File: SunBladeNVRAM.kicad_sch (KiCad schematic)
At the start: 15 parts, among them J1 Conn_01x14_Pin, J105 Conn_01x01_Pin, J106 Conn_01x01_Pin, J107 Conn_01x01_Pin, J108 Conn_01x01_Pin, J2 Conn_01x14_Pin, J3 Conn_01x02_Pin, J4 Conn_01x02_Pin, J5 Conn_01x01_Pin, J6 Conn_01x01_Pin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

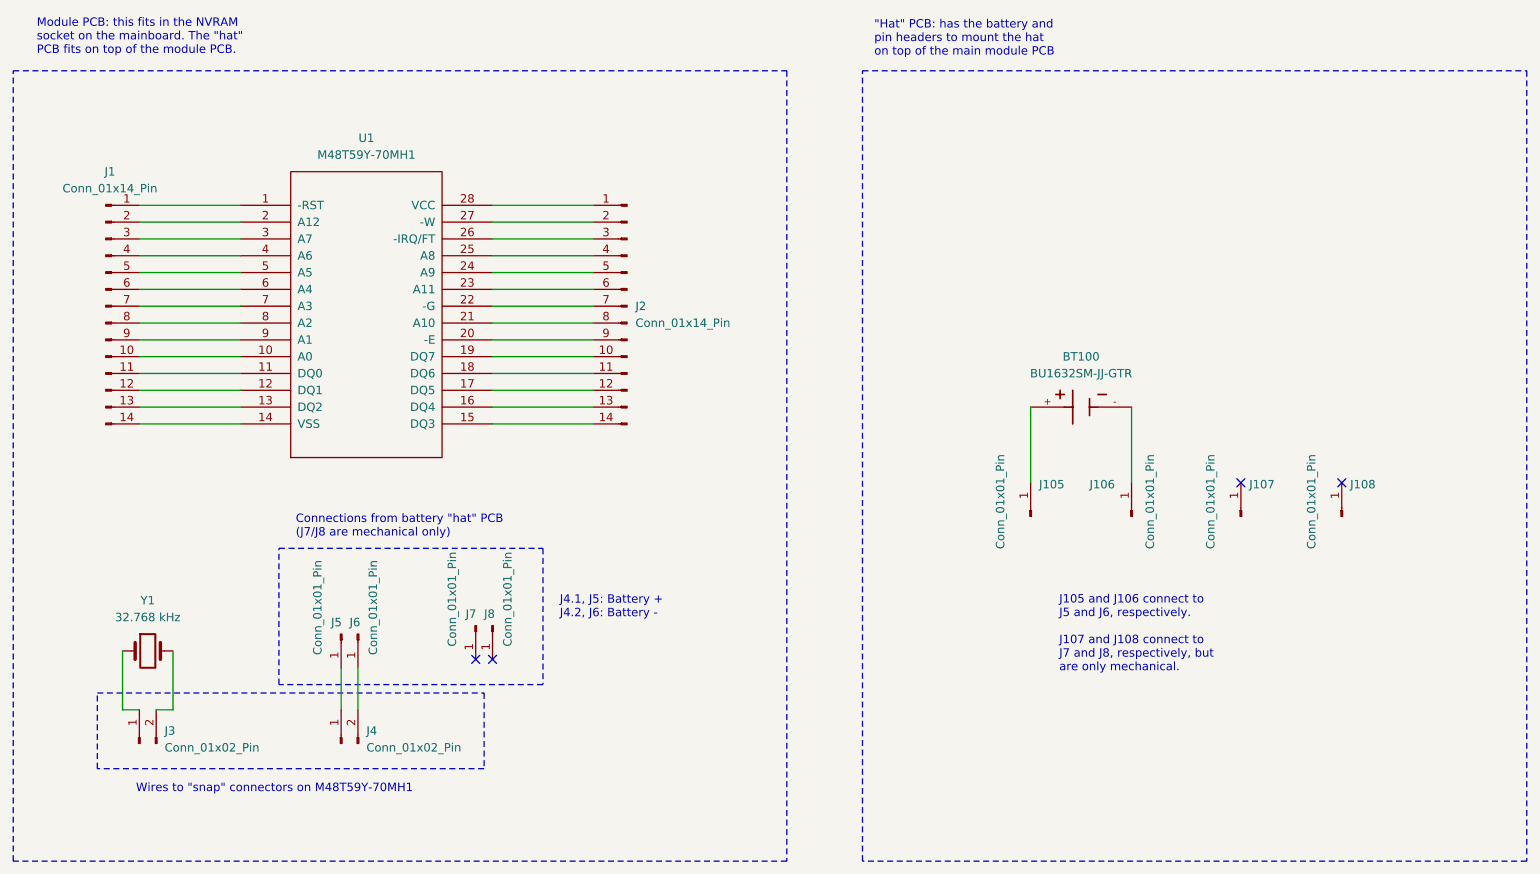
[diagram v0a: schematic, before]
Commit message: use correct M48T59Y-MH footprint
Changed pin headers to be surface mount, meaning the
pads can be on the bottom and so not interfere with the
M49T59Y.

Bottom PCB needs to be a bit larger, and the top
(battery hat) PCB also needed a minor redesign.

Still need to route the connections.
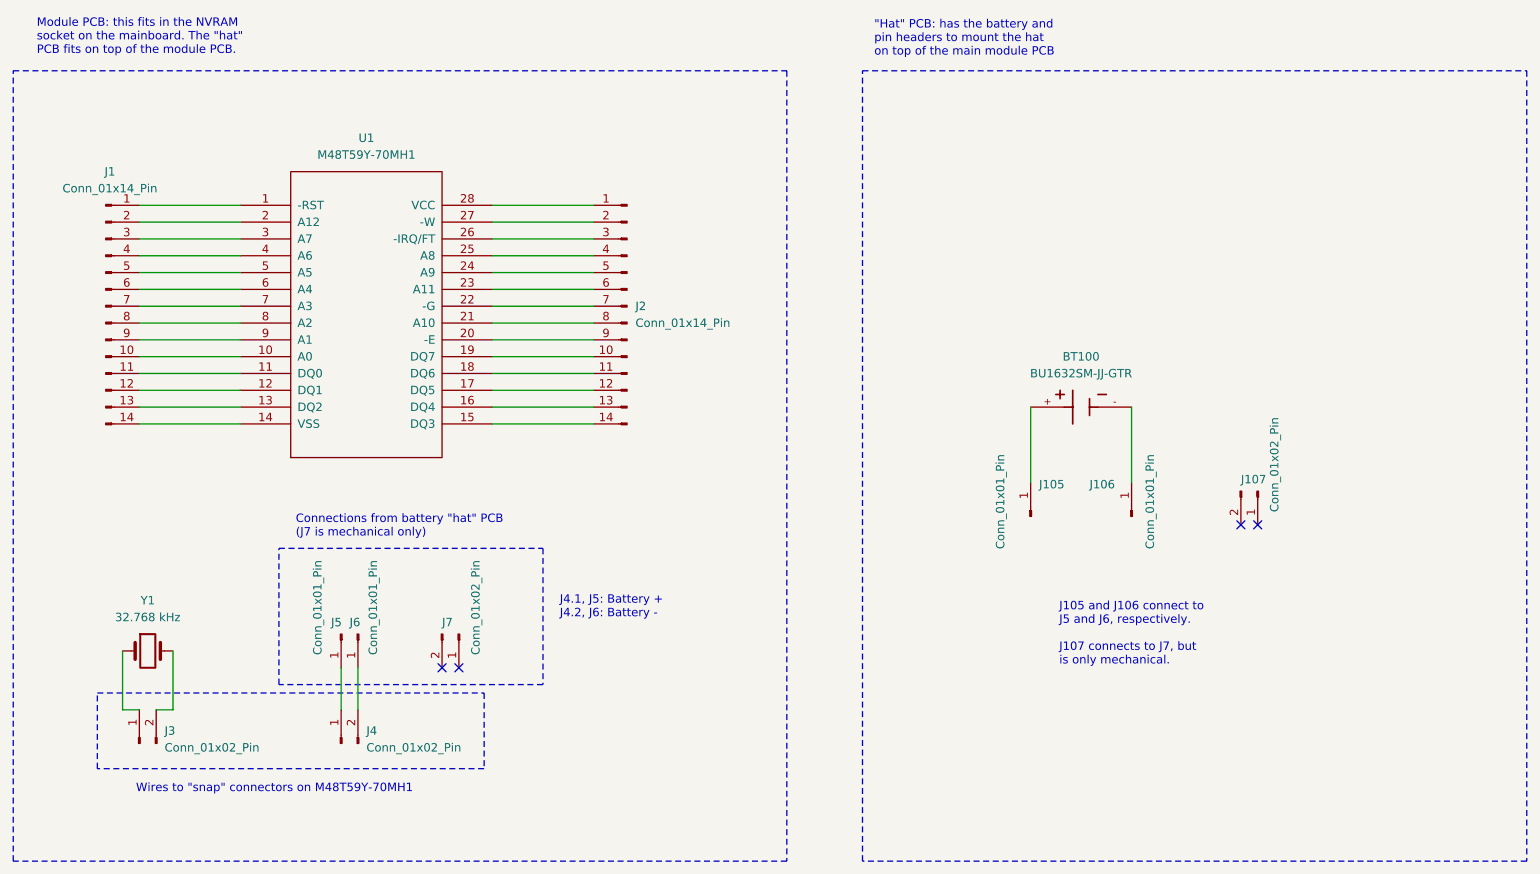
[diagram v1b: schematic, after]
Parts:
- removed J107, J108, J7, J8: Conn_01x01_Pin, Connector_PinHeader_2.54mm:PinHeader_1x01_P2.54mm_Vertical, symbol Connector:Conn_01x01_Pin
- added J107, J7: Conn_01x02_Pin, Connector_PinHeader_2.54mm:PinHeader_1x02_P2.54mm_Vertical, symbol Connector:Conn_01x02_Pin
- J1: footprint Connector_PinHeader_2.54mm:PinHeader_1x14_P2.54mm_Vertical -> Connector_PinHeader_2.54mm:PinHeader_1x14_P2.54mm_Vertical_SMD_Pin1Left
- J2: footprint Connector_PinHeader_2.54mm:PinHeader_1x14_P2.54mm_Vertical -> Connector_PinHeader_2.54mm:PinHeader_1x14_P2.54mm_Vertical_SMD_Pin1Right
- U1: footprint Package_SO:SOIC-28W_7.5x17.9mm_P1.27mm -> SunBladeNVRAM:M48T59Y-MH
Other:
- note added: "Connections from battery "hat" PCB (J7 is mechanical only)"
- note added: "J105 and J106 connect to J5 and J6, respectively. J107 connects to J7, but is only mechanical."
- note removed: "Connections from battery "hat" PCB (J7/J8 are mechanical only)"
- note removed: "J105 and J106 connect to J5 and J6, respectively. J107 and J108 connect to J7 and J8, respectively, but are only mechanical."
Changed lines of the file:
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@@
 	)
 	(no_connect
-		(at 102.87 132.08)
+		(at 215.9 111.76)
 	)
 	(no_connect
-		(at 215.9 105.41)
+		(at 218.44 111.76)
 	)
 	(no_connect
-		(at 231.14 105.41)
+		(at 95.25 133.35)
 	)
 	(no_connect
-		(at 100.33 132.08)
+		(at 97.79 133.35)
 	)
 	(wire
@@
 		)
 	)
-	(text "Connections from battery \"hat\" PCB\n(J7/J8 are mechanical only)"
+	(text "Connections from battery \"hat\" PCB\n(J7 is mechanical only)"
 		(exclude_from_sim no)
 		(at 73.152 112.014 0)
@@
 		)
 	)
-	(text "J105 and J106 connect to\nJ5 and J6, respectively.\n\nJ107 and J108 connect to\nJ7 and J8, respectively, but\nare only mechanical."
+	(text "J105 and J106 connect to\nJ5 and J6, respectively.\n\nJ107 connects to J7, but\nis only mechanical."
 		(exclude_from_sim no)
 		(at 188.468 128.27 0)
@@
 			)
 		)
-		(property "Footprint" "Connector_PinHeader_2.54mm:PinHeader_1x14_P2.54mm_Vertical"
+		(property "Footprint" "Connector_PinHeader_2.54mm:PinHeader_1x14_P2.54mm_Vertical_SMD_Pin1Left"
 			(at 44.45 78.74 0)
 			(effects
@@
 	)
 	(symbol
-		(lib_id "Connector:Conn_01x01_Pin")
-		(at 215.9 110.49 90)
+		(lib_id "Connector:Conn_01x02_Pin")
+		(at 218.44 106.68 270)
 		(unit 1)
 		(exclude_from_sim no)
@@
 		(dnp no)
 		(property "Reference" "J107"
-			(at 217.17 105.664 90)
-			(effects
-				(font
-					(size 1.27 1.27)
-				)
-				(justify right)
-			)
-		)
-		(property "Value" "Conn_01x01_Pin"
-			(at 211.328 101.092 0)
-			(effects
-				(font
-					(size 1.27 1.27)
-				)
-				(justify right)
-			)
-		)
-		(property "Footprint" "Connector_PinHeader_2.54mm:PinHeader_1x01_P2.54mm_Vertical"
-			(at 215.9 110.49 0)
+			(at 215.9 104.902 90)
+			(effects
+				(font
+					(size 1.27 1.27)
+				)
+				(justify left)
+			)
+		)
+		(property "Value" "Conn_01x02_Pin"
+			(at 220.98 95.504 0)
+			(effects
+				(font
+					(size 1.27 1.27)
+				)
+				(justify left)
+			)
+		)
+		(property "Footprint" "Connector_PinHeader_2.54mm:PinHeader_1x02_P2.54mm_Vertical"
+			(at 218.44 106.68 0)
 			(effects
 				(font
@@
 		)
 		(property "Datasheet" "~"
-			(at 215.9 110.49 0)
-			(effects
-				(font
-					(size 1.27 1.27)
-				)
-				(hide yes)
-			)
-		)
-		(property "Description" "Generic connector, single row, 01x01, script generated"
-			(at 215.9 110.49 0)
+			(at 218.44 106.68 0)
+			(effects
+				(font
+					(size 1.27 1.27)
+				)
+				(hide yes)
+			)
+		)
+		(property "Description" "Generic connector, single row, 01x02, script generated"
+			(at 218.44 106.68 0)
 			(effects
 				(font
@@
 		)
 		(pin "1"
+		)
+		(pin "2"
 		)
 		(instances
@@
 				(path "/a5619b9c-2a1e-4dd3-8c34-92032ec8ab73"
 					(reference "J107")
-					(unit 1)
-				)
-			)
-		)
-	)
-	(symbol
-		(lib_id "Connector:Conn_01x01_Pin")
-		(at 231.14 110.49 90)
-		(unit 1)
-		(exclude_from_sim no)
-		(in_bom yes)
-		(on_board yes)
-		(dnp no)
-		(property "Reference" "J108"
-			(at 232.41 105.664 90)
-			(effects
-				(font
-					(size 1.27 1.27)
-				)
-				(justify right)
-			)
-		)
-		(property "Value" "Conn_01x01_Pin"
-			(at 226.568 101.092 0)
-			(effects
-				(font
-					(size 1.27 1.27)
-				)
-				(justify right)
-			)
-		)
-		(property "Footprint" "Connector_PinHeader_2.54mm:PinHeader_1x01_P2.54mm_Vertical"
-			(at 231.14 110.49 0)
-			(effects
-				(font
-					(size 1.27 1.27)
-				)
-				(hide yes)
-			)
-		)
-		(property "Datasheet" "~"
-			(at 231.14 110.49 0)
-			(effects
-				(font
-					(size 1.27 1.27)
-				)
-				(hide yes)
-			)
-		)
-		(property "Description" "Generic connector, single row, 01x01, script generated"
-			(at 231.14 110.49 0)
-			(effects
-				(font
-					(size 1.27 1.27)
-				)
-				(hide yes)
-			)
-		)
-		(pin "1"
-		)
-		(instances
-			(project "SunBladeNVRAM"
-				(path "/a5619b9c-2a1e-4dd3-8c34-92032ec8ab73"
-					(reference "J108")
 					(unit 1)
 				)
@@
 	(symbol
 		(lib_id "Connector:Conn_01x01_Pin")
-		(at 100.33 127 270)
-		(unit 1)
-		(exclude_from_sim no)
-		(in_bom yes)
-		(on_board yes)
-		(dnp no)
-		(property "Reference" "J7"
-			(at 98.806 125.222 90)
-			(effects
-				(font
-					(size 1.27 1.27)
-				)
-				(justify left)
-			)
-		)
-		(property "Value" "Conn_01x01_Pin"
-			(at 96.774 115.824 0)
-			(effects
-				(font
-					(size 1.27 1.27)
-				)
-				(justify left)
-			)
-		)
-		(property "Footprint" "Connector_PinHeader_2.54mm:PinHeader_1x01_P2.54mm_Vertical"
-			(at 100.33 127 0)
-			(effects
-				(font
-					(size 1.27 1.27)
-				)
-				(hide yes)
-			)
-		)
-		(property "Datasheet" "~"
-			(at 100.33 127 0)
-			(effects
-				(font
-					(size 1.27 1.27)
-				)
-				(hide yes)
-			)
-		)
-		(property "Description" "Generic connector, single row, 01x01, script generated"
-			(at 100.33 127 0)
-			(effects
-				(font
-					(size 1.27 1.27)
-				)
-				(hide yes)
-			)
-		)
-		(pin "1"
-		)
-		(instances
-			(project "SunBladeNVRAM"
-				(path "/a5619b9c-2a1e-4dd3-8c34-92032ec8ab73"
-					(reference "J7")
-					(unit 1)
-				)
-			)
-		)
-	)
-	(symbol
-		(lib_id "Connector:Conn_01x01_Pin")
-		(at 102.87 127 270)
-		(unit 1)
-		(exclude_from_sim no)
-		(in_bom yes)
-		(on_board yes)
-		(dnp no)
-		(property "Reference" "J8"
-			(at 101.6 125.222 90)
-			(effects
-				(font
-					(size 1.27 1.27)
-				)
-				(justify left)
-			)
-		)
-		(property "Value" "Conn_01x01_Pin"
-			(at 105.156 115.824 0)
-			(effects
-				(font
-					(size 1.27 1.27)
-				)
-				(justify left)
-			)
-		)
-		(property "Footprint" "Connector_PinHeader_2.54mm:PinHeader_1x01_P2.54mm_Vertical"
-			(at 102.87 127 0)
-			(effects
-				(font
-					(size 1.27 1.27)
-				)
-				(hide yes)
-			)
-		)
-		(property "Datasheet" "~"
-			(at 102.87 127 0)
-			(effects
-				(font
-					(size 1.27 1.27)
-				)
-				(hide yes)
-			)
-		)
-		(property "Description" "Generic connector, single row, 01x01, script generated"
-			(at 102.87 127 0)
-			(effects
-				(font
-					(size 1.27 1.27)
-				)
-				(hide yes)
-			)
-		)
-		(pin "1"
-		)
-		(instances
-			(project "SunBladeNVRAM"
-				(path "/a5619b9c-2a1e-4dd3-8c34-92032ec8ab73"
-					(reference "J8")
-					(unit 1)
-				)
-			)
-		)
-	)
-	(symbol
-		(lib_id "Connector:Conn_01x01_Pin")
 		(at 184.15 110.49 90)
 		(unit 1)
@@
 			)
 		)
-		(property "Footprint" "Connector_PinHeader_2.54mm:PinHeader_1x14_P2.54mm_Vertical"
+		(property "Footprint" "Connector_PinHeader_2.54mm:PinHeader_1x14_P2.54mm_Vertical_SMD_Pin1Right"
 			(at 123.19 78.74 0)
 			(effects
@@
 			)
 		)
-		(property "Footprint" "Package_SO:SOIC-28W_7.5x17.9mm_P1.27mm"
+		(property "Footprint" "SunBladeNVRAM:M48T59Y-MH"
 			(at 83.82 80.01 0)
 			(effects
@@
 					(unit 1)
 				)
+			)
+		)
+	)
+	(symbol
+		(lib_id "Connector:Conn_01x02_Pin")
+		(at 97.79 128.27 270)
+		(unit 1)
+		(exclude_from_sim no)
+		(in_bom yes)
+		(on_board yes)
+		(dnp no)
+		(property "Reference" "J7"
+			(at 95.25 126.492 90)
+			(effects
+				(font
+					(size 1.27 1.27)
+				)
+				(justify left)
+			)
+		)
+		(property "Value" "Conn_01x02_Pin"
+			(at 100.33 117.094 0)
+			(effects
+				(font
+					(size 1.27 1.27)
+				)
+				(justify left)
+			)
+		)
+		(property "Footprint" "Connector_PinHeader_2.54mm:PinHeader_1x02_P2.54mm_Vertical"
+			(at 97.79 128.27 0)
+			(effects
+				(font
+					(size 1.27 1.27)
+				)
+				(hide yes)
+			)
+		)
+		(property "Datasheet" "~"
+			(at 97.79 128.27 0)
+			(effects
+				(font
+					(size 1.27 1.27)
+				)
+				(hide yes)
+			)
+		)
+		(property "Description" "Generic connector, single row, 01x02, script generated"
+			(at 97.79 128.27 0)
+			(effects
+				(font
+					(size 1.27 1.27)
+				)
+				(hide yes)
+			)
+		)
+		(pin "1"
+		)
+		(pin "2"
+		)
+		(instances
+			(project ""
+				(path "/a5619b9c-2a1e-4dd3-8c34-92032ec8ab73"
+					(reference "J7")
+					(unit 1)
+				)
